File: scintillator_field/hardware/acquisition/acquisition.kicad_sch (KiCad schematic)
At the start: 0 parts

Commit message: usb-c
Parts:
- added C1: 100n, symbol Device:C
- added J1: USB_C_16P_F, symbol Connector:USB_C_Receptacle_USB2.0_16P
- added R1: 0R, symbol Device:R
- added R2, R3: 5k1, symbol Device:R
- added U10: USBLC6-2SC6, Package_TO_SOT_SMD:SOT-23-6, symbol Power_Protection:USBLC6-2SC6
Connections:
- new net: J1.A7 (D-), J1.B7 (D-), U10.1 (I/O1)
- new net: J1.A6 (D+), J1.B6 (D+), U10.3 (I/O2)
- new net: J1.A5 (CC1), R2.1
- new net: J1.B5 (CC2), R3.1
- new net +5V: R1.2
- new net GND: C1.2, J1.A1 (GND), J1.A12 (GND), J1.B1 (GND), J1.B12 (GND), J1.S1 (SHIELD), R2.2, R3.2, U10.2 (GND)
- new net VBUS: C1.1, J1.A4 (VBUS), J1.A9 (VBUS), J1.B4 (VBUS), J1.B9 (VBUS), R1.1, U10.5 (VBUS)
- new net mcu/USBC_D_N: U10.6 (I/O1)
- new net mcu/USBC_D_P: U10.4 (I/O2)
- no-connect marks 0 -> 2
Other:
- sheet mcu ports: added USBC_D_N, USBC_D_P; removed none

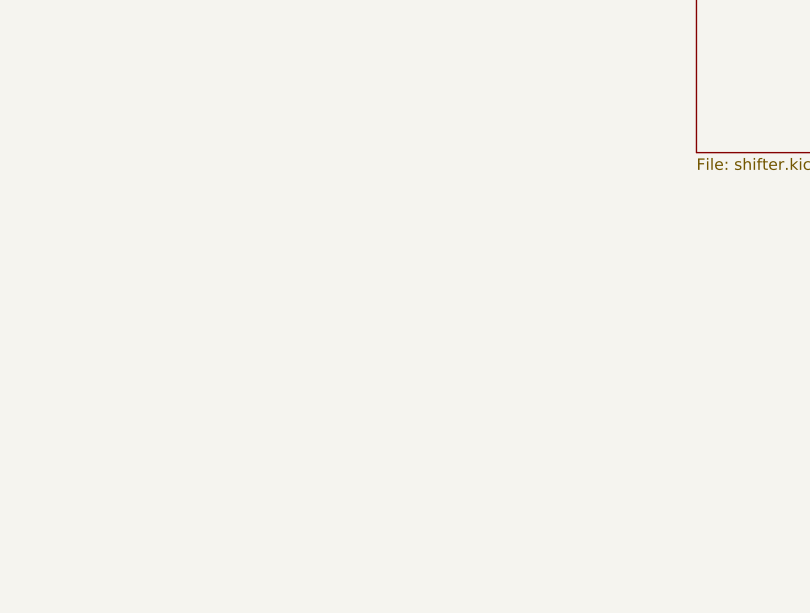
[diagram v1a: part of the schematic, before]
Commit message: pins of registers
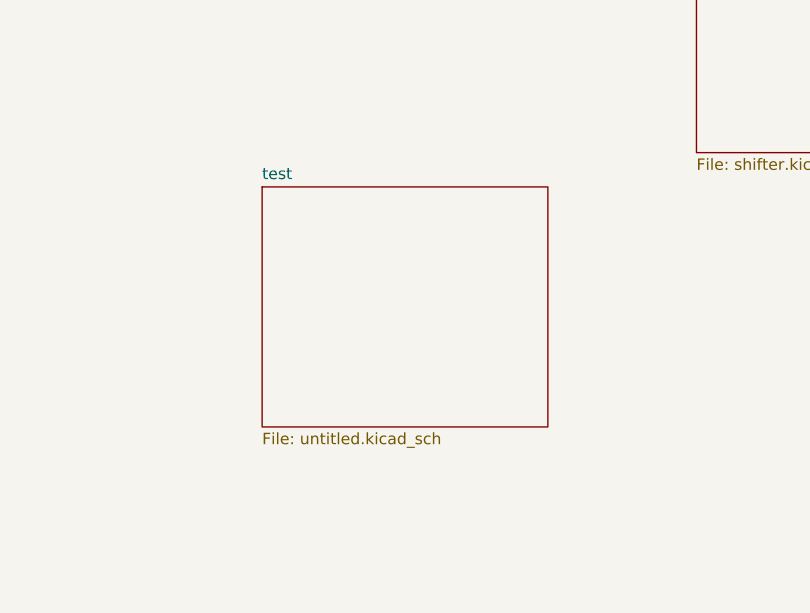
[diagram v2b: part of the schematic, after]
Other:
- added sheet test (untitled.kicad_sch)
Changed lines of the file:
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@@
+	)
+	(sheet
+		(at 143.51 104.14)
+		(size 31.75 26.67)
+		(fields_autoplaced yes)
+		(stroke
+			(width 0.1524)
+			(type solid)
+		)
+		(fill
+			(color 0 0 0 0.0000)
+		)
+		(property "Sheetname" "test"
+			(at 143.51 103.4284 0)
+			(effects
+				(font
+					(size 1.27 1.27)
+				)
+				(justify left bottom)
+			)
+		)
+		(property "Sheetfile" "untitled.kicad_sch"
+			(at 143.51 131.3946 0)
+			(effects
+				(font
+					(size 1.27 1.27)
+				)
+				(justify left top)
+			)
+		)
+		(instances
+			(project "acquisition"
+				(path "/dd68efff-541d-4422-8da3-c773bf0d34e4"
+					(page "6")
+				)
+			)
+		)
 	)
 	(sheet
